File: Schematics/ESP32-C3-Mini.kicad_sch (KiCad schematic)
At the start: 13 parts, among them J7 USB_C_Receptacle, U4 ESP32-C3-MINI-1-N4, U6 LDL1117-3.3

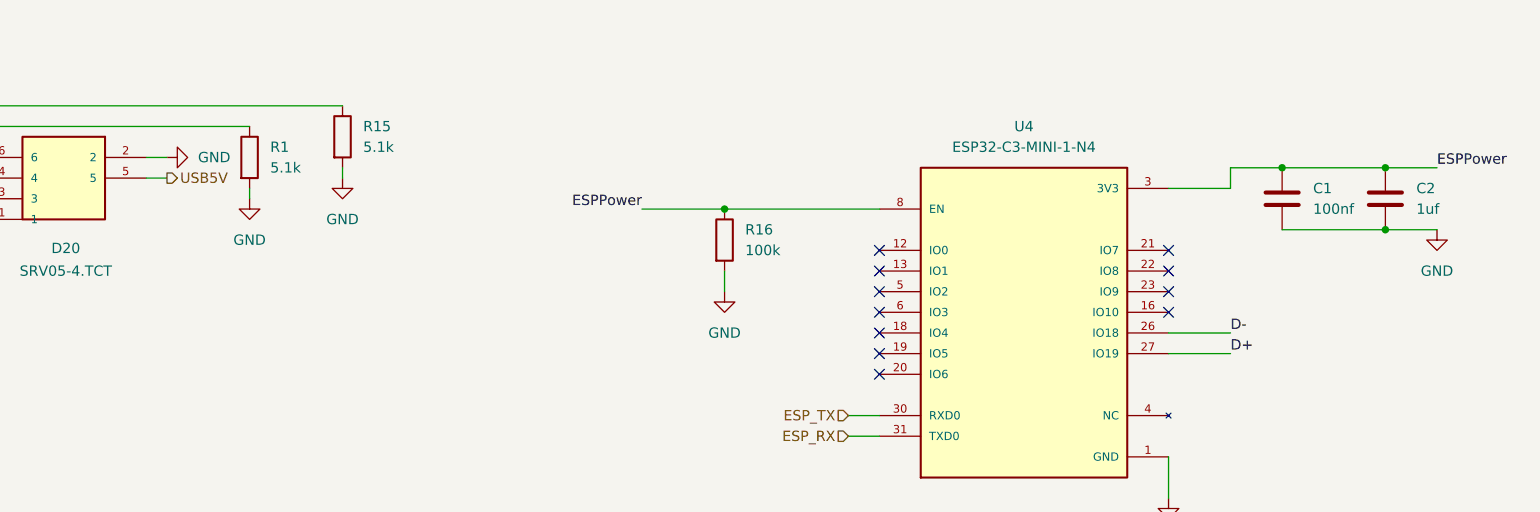
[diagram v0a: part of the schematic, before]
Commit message: finished first layout and routing
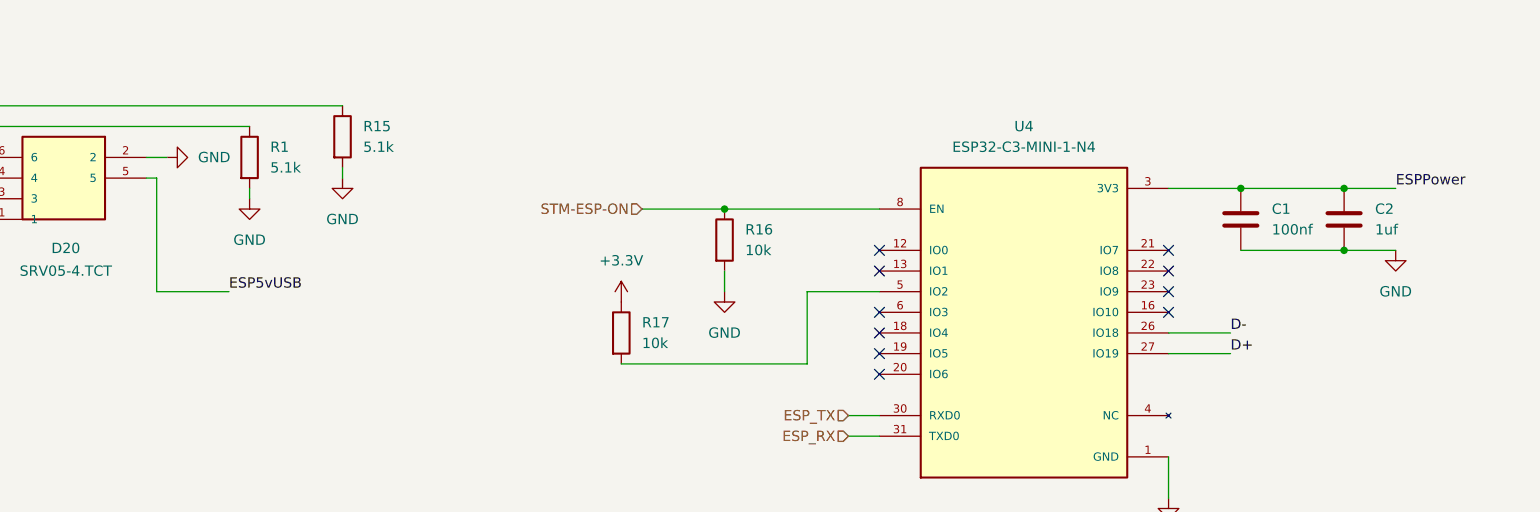
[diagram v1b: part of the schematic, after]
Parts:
- added R17: 10k, Resistor_SMD:R_0805_2012Metric_Pad1.20x1.40mm_HandSolder, symbol Device:R
- R16: value 100k -> 10k; footprint (none) -> Resistor_SMD:R_0805_2012Metric_Pad1.20x1.40mm_HandSolder
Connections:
- net USB5V is gone; now on net ESP5vUSB: D20.5
- net ESPPower: no longer R16.1, U4.8 (EN)
- net at U4.5 (IO2): now also R17.2
- new net +3.3V: R17.1
- new net STM-ESP-ON: R16.1, U4.8 (EN)
- no-connect marks 24 -> 23
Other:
- moved on the sheet: C1, C2

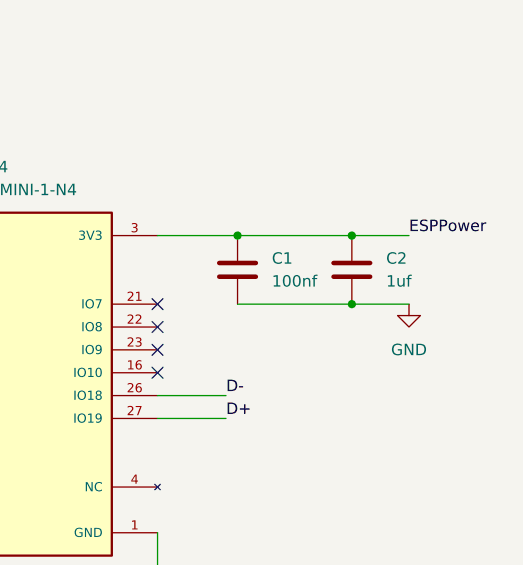
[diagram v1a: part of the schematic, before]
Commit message: clean up of routing
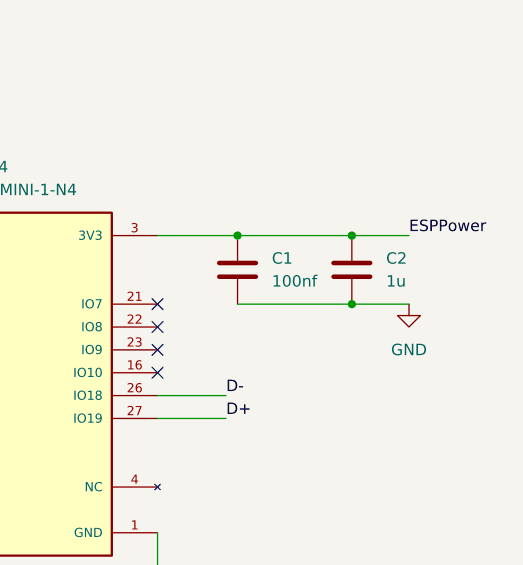
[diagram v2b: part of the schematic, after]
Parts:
- C1: LCSC (none) -> C49678
- C2: value 1uf -> 1u; LCSC (none) -> C28323
- R16, R17: LCSC C96346 -> C84376
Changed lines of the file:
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@@
 			)
 		)
-		(property "LCSC" "C96346"
+		(property "LCSC" "C84376"
 			(at 151.13 66.04 0)
 			(effects
@@
 			)
 		)
+		(property "LCSC" "C49678"
+			(at 227.33 52.07 0)
+			(effects
+				(font
+					(size 1.27 1.27)
+				)
+				(hide yes)
+			)
+		)
 		(pin "1"
 		)
@@
 			)
 		)
-		(property "Value" "1uf"
+		(property "Value" "1u"
 			(at 243.84 53.3399 0)
 			(effects
@@
 		)
 		(property "Description" "Unpolarized capacitor"
+			(at 240.03 52.07 0)
+			(effects
+				(font
+					(size 1.27 1.27)
+				)
+				(hide yes)
+			)
+		)
+		(property "LCSC" "C28323"
 			(at 240.03 52.07 0)
 			(effects
@@
 			)
 		)
-		(property "LCSC" "C96346"
+		(property "LCSC" "C84376"
 			(at 163.83 54.61 0)
 			(effects

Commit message: updated board waiting on review
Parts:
- D20: DESCRIPTION Semtech SRV05-4.TCT, Uni-Directional TVS Diode Array, 300W,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 -> (none)
